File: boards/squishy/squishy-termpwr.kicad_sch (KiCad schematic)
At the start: 23 parts, among them J7 syzygy_standard_x1, Q3 Q_NMOS_PMOS_D1G2S2D2G1S1, U1 LFE5U-45F-8BG256, U11 AD7091R-5, U12 INAx180

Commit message: hardware: cleaned up the schematics a bit and made them more unified
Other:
- company: (none) -> Shrine Maiden Heavy Industries
- title: (none) -> Squishy - Multitool - Termination Power / Expansion
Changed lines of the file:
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@@
 (kicad_sch (version 20211123) (generator eeschema)
-  (paper "A4")
+  (paper "A3")
+  (title_block
+    (title "Squishy - Multitool - Termination Power / Expansion")
+    (date "2021-12-21")
+    (rev "2")
+    (company "Shrine Maiden Heavy Industries")
+    (comment 1 "License:  CERN-OHL-S")
+    (comment 2 "© 2020 Aki 'lethalbit' Van Ness, et. al.")
+    (comment 3 "SCSI PHY Termination power managment and expansion header")
+    (comment 4 "Squishy - SCSI multitool and gateware library")
+  )
   (junction (at 21.59 66.04) (diameter 0) (color 0 0 0 0)
   )

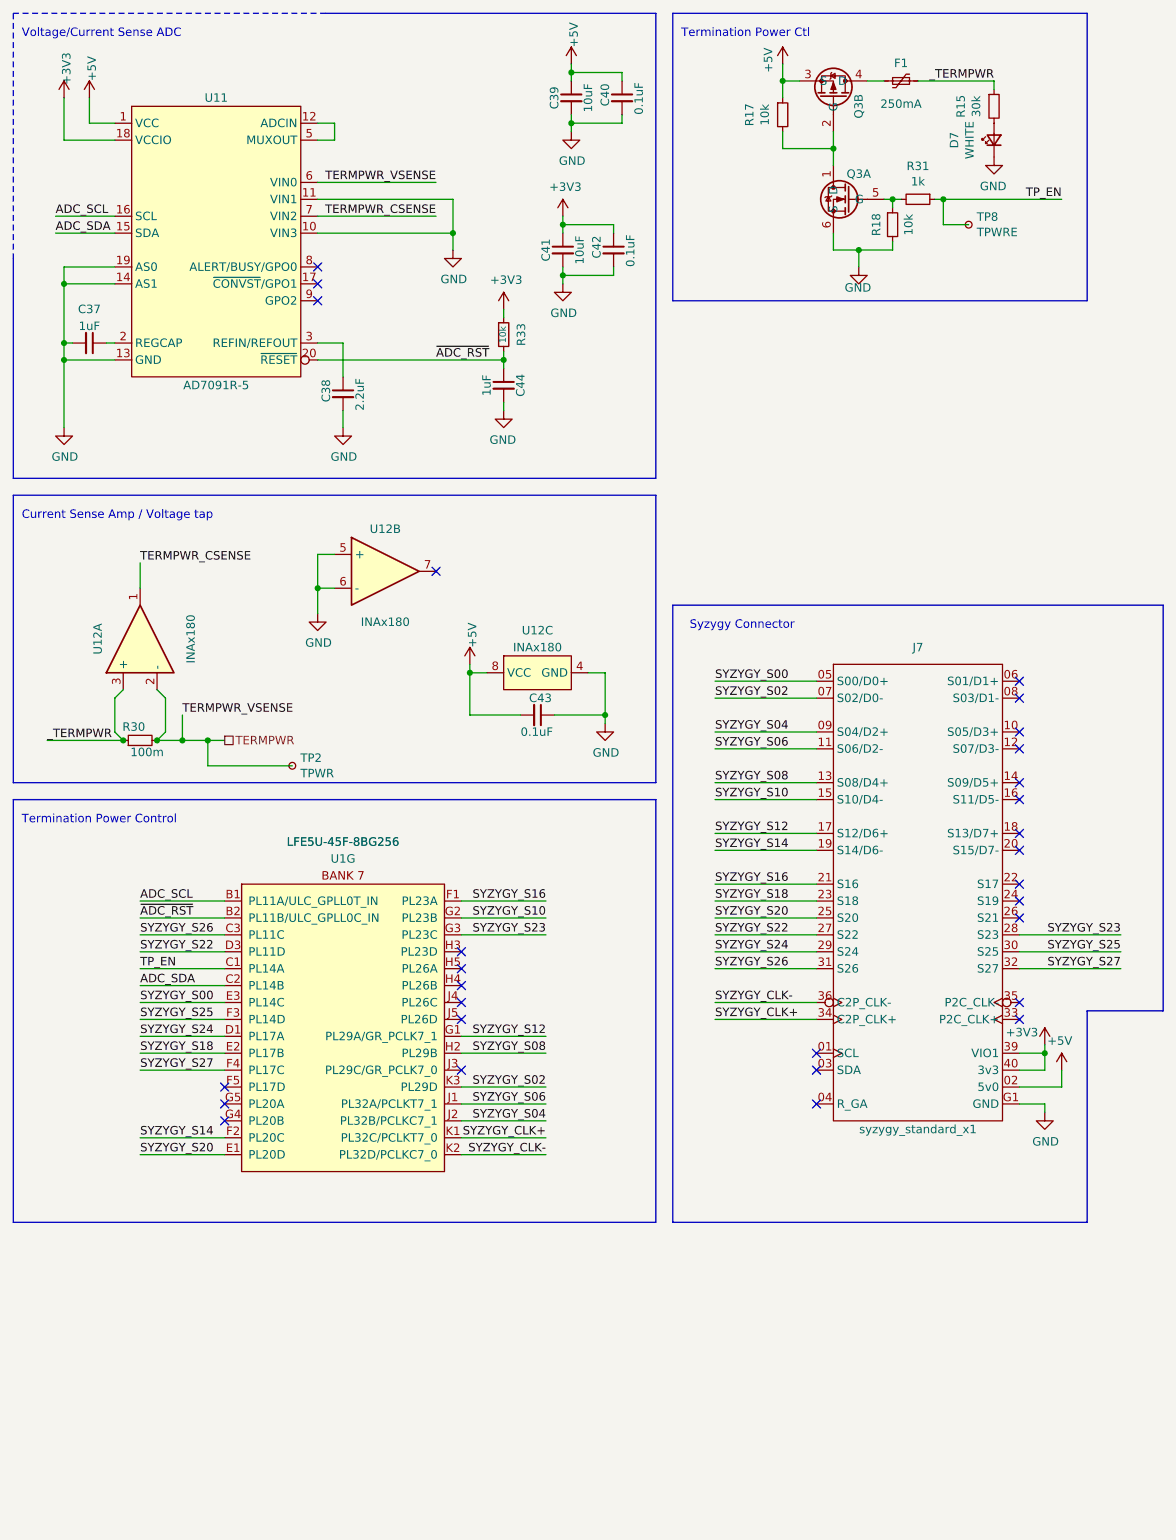
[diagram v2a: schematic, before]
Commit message: hardware: removed the syszygy connector
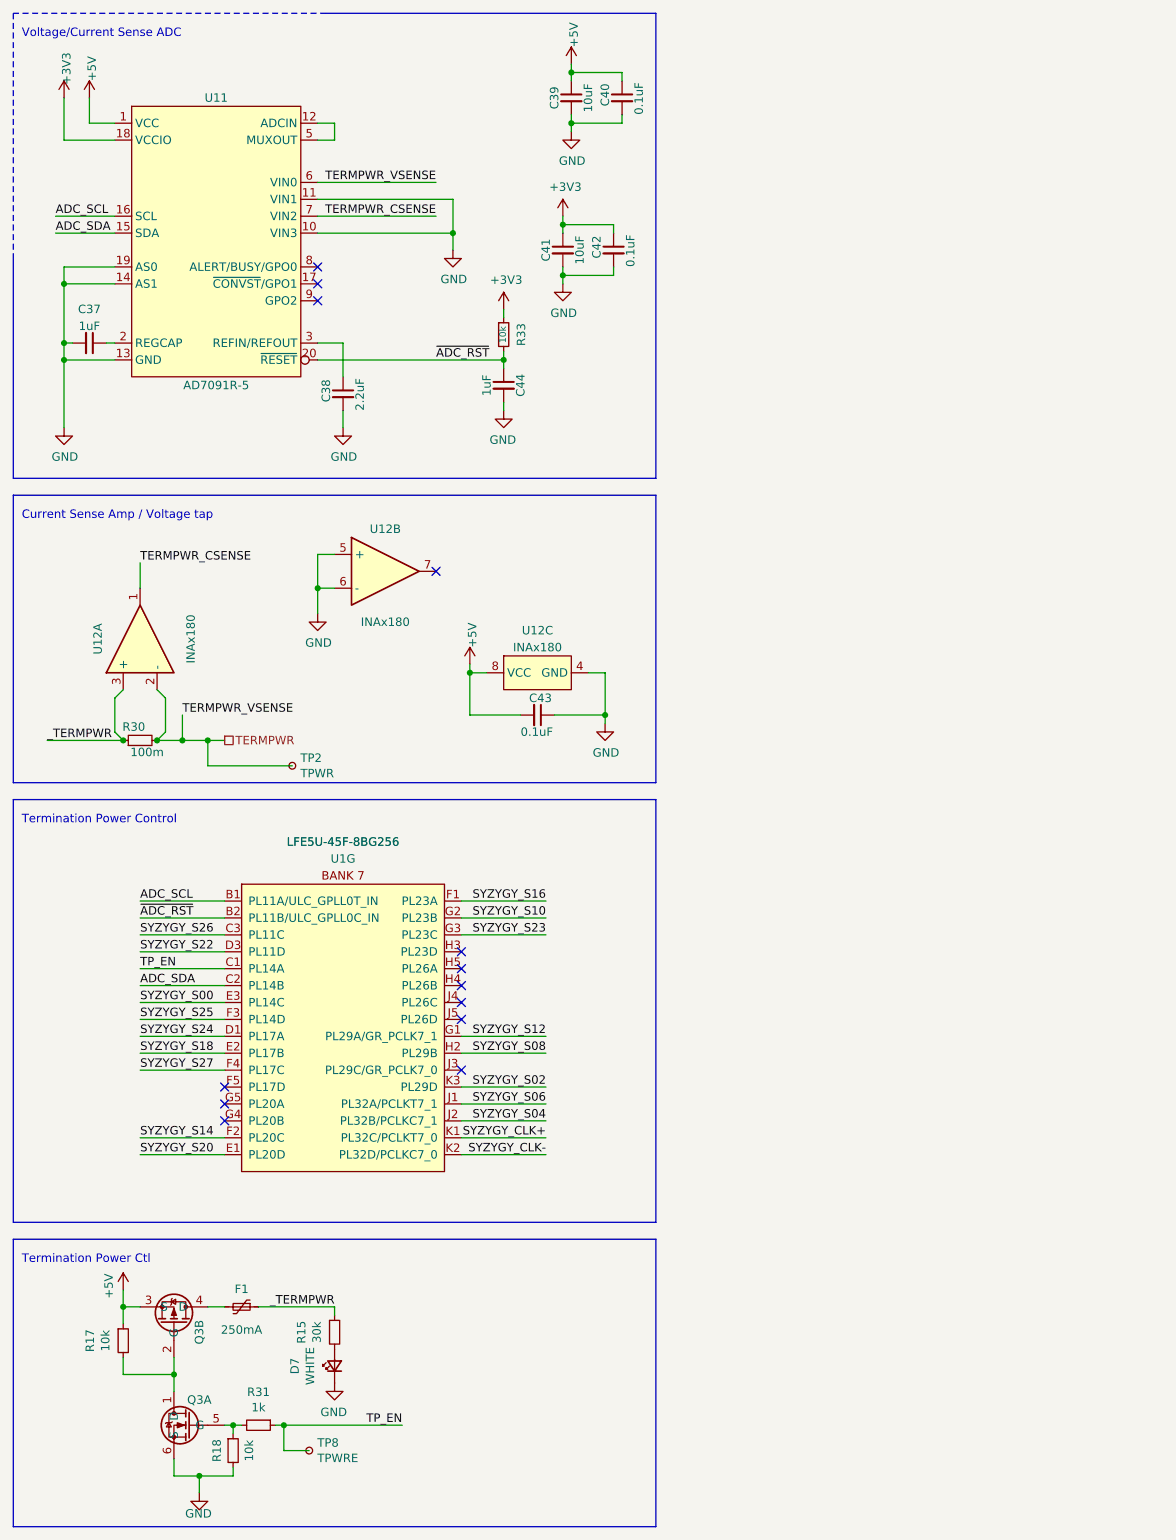
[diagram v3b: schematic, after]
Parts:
- removed J7: syzygy_standard_x1, lethalbit-connectors:syzygy_standard_x1, symbol lethalbit-connectors:syzygy_standard_x1
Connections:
- no-connect marks 29 -> 13
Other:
- note removed: "Syzygy Connector"
- moved on the sheet: D7, F1, Q3A, Q3B, R15, R17, R18, R31, TP8

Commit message: hardware: update fuse symbol footprint
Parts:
- F1: footprint Fuse:Fuse_1210_3225Metric_Castellated -> Fuse:Fuse_1210_3225Metric
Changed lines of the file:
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@@
     (property "Reference" "F1" (id 0) (at 48.26 205.613 90))
     (property "Value" "250mA" (id 1) (at 48.26 211.7344 90))
-    (property "Footprint" "Fuse:Fuse_1210_3225Metric_Castellated" (id 2) (at 43.18 209.55 0)
+    (property "Footprint" "Fuse:Fuse_1210_3225Metric" (id 2) (at 43.18 209.55 0)
       (effects (font (size 1.27 1.27)) (justify left) hide)
     )

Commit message: hardware: some ERC cleanup
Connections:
- net SYZYGY_CLK+: no longer names the net of U1.K1 (PL32C/PCLKT7_0)
- net SYZYGY_CLK-: no longer names the net of U1.K2 (PL32D/PCLKC7_0)
- net SYZYGY_S00: no longer names the net of U1.E3 (PL14C)
- net SYZYGY_S02: no longer names the net of U1.K3 (PL29D)
- net SYZYGY_S04: no longer names the net of U1.J2 (PL32B/PCLKC7_1)
- net SYZYGY_S06: no longer names the net of U1.J1 (PL32A/PCLKT7_1)
- net SYZYGY_S08: no longer names the net of U1.H2 (PL29B)
- net SYZYGY_S10: no longer names the net of U1.G2 (PL23B)
- net SYZYGY_S12: no longer names the net of U1.G1 (PL29A/GR_PCLK7_1)
- net SYZYGY_S14: no longer names the net of U1.F2 (PL20C)
- net SYZYGY_S16: no longer names the net of U1.F1 (PL23A)
- net SYZYGY_S18: no longer names the net of U1.E2 (PL17B)
- net SYZYGY_S20: no longer names the net of U1.E1 (PL20D)
- net SYZYGY_S22: no longer names the net of U1.D3 (PL11D)
- net SYZYGY_S23: no longer names the net of U1.G3 (PL23C)
- net SYZYGY_S24: no longer names the net of U1.D1 (PL17A)
- net SYZYGY_S25: no longer names the net of U1.F3 (PL14D)
- net SYZYGY_S26: no longer names the net of U1.C3 (PL11C)
- net SYZYGY_S27: no longer names the net of U1.F4 (PL17C)
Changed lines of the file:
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@@
-    (stroke (width 0) (type default) (color 0 0 0 0))
-  )
-  (wire (pts (xy 93.98 147.32) (xy 81.28 147.32))
     (stroke (width 0) (type default) (color 0 0 0 0))
   )
@@
     (stroke (width 0) (type default) (color 0 0 0 0))
   )
-  (wire (pts (xy 93.98 167.64) (xy 81.28 167.64))
-    (stroke (width 0) (type default) (color 0 0 0 0))
-  )
   (wire (pts (xy 63.5 63.5) (xy 63.5 68.58))
     (stroke (width 0) (type default) (color 0 0 0 0))
@@
     (stroke (width 0) (type solid) (color 0 0 0 0))
   )
-  (wire (pts (xy 33.02 167.64) (xy 45.72 167.64))
-    (stroke (width 0) (type default) (color 0 0 0 0))
-  )
-  (wire (pts (xy 33.02 170.18) (xy 45.72 170.18))
-    (stroke (width 0) (type default) (color 0 0 0 0))
-  )
   (wire (pts (xy 35.56 123.19) (xy 36.83 121.92))
     (stroke (width 0) (type default) (color 0 0 0 0))
@@
     (stroke (width 0) (type default) (color 0 0 0 0))
   )
-  (wire (pts (xy 93.98 152.4) (xy 81.28 152.4))
-    (stroke (width 0) (type default) (color 0 0 0 0))
-  )
-  (wire (pts (xy 33.02 152.4) (xy 45.72 152.4))
-    (stroke (width 0) (type default) (color 0 0 0 0))
-  )
   (wire (pts (xy 21.59 54.61) (xy 21.59 63.5))
     (stroke (width 0) (type default) (color 0 0 0 0))
   )
-  (wire (pts (xy 81.28 185.42) (xy 93.98 185.42))
-    (stroke (width 0) (type default) (color 0 0 0 0))
-  )
   (wire (pts (xy 97.79 22.86) (xy 97.79 24.13))
     (stroke (width 0) (type default) (color 0 0 0 0))
@@
     (stroke (width 0) (type default) (color 0 0 0 0))
   )
-  (wire (pts (xy 93.98 180.34) (xy 81.28 180.34))
-    (stroke (width 0) (type default) (color 0 0 0 0))
-  )
   (wire (pts (xy 21.59 63.5) (xy 22.86 63.5))
     (stroke (width 0) (type default) (color 0 0 0 0))
@@
     (stroke (width 0) (type default) (color 0 0 0 0))
   )
-  (wire (pts (xy 33.02 182.88) (xy 45.72 182.88))
-    (stroke (width 0) (type default) (color 0 0 0 0))
-  )
   (wire (pts (xy 30.48 208.28) (xy 30.48 205.74))
     (stroke (width 0) (type solid) (color 0 0 0 0))
@@
     (stroke (width 0) (type default) (color 0 0 0 0))
   )
-  (wire (pts (xy 33.02 165.1) (xy 45.72 165.1))
-    (stroke (width 0) (type default) (color 0 0 0 0))
-  )
   (wire (pts (xy 20.32 44.45) (xy 29.21 44.45))
     (stroke (width 0) (type default) (color 0 0 0 0))
@@
     (stroke (width 0) (type default) (color 0 0 0 0))
   )
-  (wire (pts (xy 33.02 154.94) (xy 45.72 154.94))
-    (stroke (width 0) (type default) (color 0 0 0 0))
-  )
-  (wire (pts (xy 33.02 185.42) (xy 45.72 185.42))
-    (stroke (width 0) (type default) (color 0 0 0 0))
-  )
   (wire (pts (xy 46.99 226.06) (xy 46.99 227.33))
     (stroke (width 0) (type default) (color 0 0 0 0))
@@
     (stroke (width 0) (type default) (color 0 0 0 0))
   )
-  (wire (pts (xy 93.98 175.26) (xy 81.28 175.26))
-    (stroke (width 0) (type default) (color 0 0 0 0))
-  )
   (wire (pts (xy 97.79 30.48) (xy 97.79 31.75))
     (stroke (width 0) (type default) (color 0 0 0 0))
@@
     (stroke (width 0) (type default) (color 0 0 0 0))
   )
-  (wire (pts (xy 93.98 149.86) (xy 81.28 149.86))
-    (stroke (width 0) (type default) (color 0 0 0 0))
-  )
   (wire (pts (xy 45.72 208.28) (xy 43.18 208.28))
     (stroke (width 0) (type solid) (color 0 0 0 0))
@@
     (stroke (width 0) (type default) (color 0 0 0 0))
   )
-  (wire (pts (xy 93.98 170.18) (xy 81.28 170.18))
-    (stroke (width 0) (type default) (color 0 0 0 0))
-  )
   (polyline (pts (xy 110.49 83.82) (xy 13.97 83.82))
     (stroke (width 0) (type default) (color 0 0 0 0))
@@
     (stroke (width 0) (type default) (color 0 0 0 0))
   )
-  (wire (pts (xy 33.02 162.56) (xy 45.72 162.56))
-    (stroke (width 0) (type default) (color 0 0 0 0))
-  )
   (wire (pts (xy 96.52 53.34) (xy 96.52 54.61))
     (stroke (width 0) (type default) (color 0 0 0 0))
@@
   )
   (wire (pts (xy 38.1 233.68) (xy 41.91 233.68))
-    (stroke (width 0) (type default) (color 0 0 0 0))
-  )
-  (wire (pts (xy 33.02 172.72) (xy 45.72 172.72))
     (stroke (width 0) (type default) (color 0 0 0 0))
   )
@@
     (stroke (width 0) (type solid) (color 0 0 0 0))
   )
-  (wire (pts (xy 81.28 182.88) (xy 93.98 182.88))
-    (stroke (width 0) (type default) (color 0 0 0 0))
-  )
   (wire (pts (xy 39.37 123.19) (xy 35.56 123.19))
     (stroke (width 0) (type default) (color 0 0 0 0))
@@
   )
   (wire (pts (xy 29.21 30.48) (xy 25.4 30.48))
-    (stroke (width 0) (type default) (color 0 0 0 0))
-  )
-  (wire (pts (xy 93.98 177.8) (xy 81.28 177.8))
     (stroke (width 0) (type default) (color 0 0 0 0))
   )
@@
     (effects (font (size 1.27 1.27)) (justify left bottom))
   )
-  (label "SYZYGY_S20" (at 33.02 185.42 0)
-    (effects (font (size 1.27 1.27)) (justify left bottom))
-  )
-  (label "SYZYGY_S14" (at 33.02 182.88 0)
-    (effects (font (size 1.27 1.27)) (justify left bottom))
-  )
-  (label "SYZYGY_CLK+" (at 93.98 182.88 180)
-    (effects (font (size 1.27 1.27)) (justify right bottom))
-  )
   (label "ADC_SCL" (at 33.02 147.32 0)
     (effects (font (size 1.27 1.27)) (justify left bottom))
@@
     (effects (font (size 1.27 1.27)) (justify right bottom))
   )
-  (label "SYZYGY_S25" (at 33.02 165.1 0)
-    (effects (font (size 1.27 1.27)) (justify left bottom))
-  )
   (label "TP_EN" (at 72.39 226.06 180)
     (effects (font (size 1.27 1.27)) (justify right bottom))
@@
     (effects (font (size 1.27 1.27)) (justify left bottom))
   )
-  (label "SYZYGY_S06" (at 93.98 177.8 180)
-    (effects (font (size 1.27 1.27)) (justify right bottom))
-  )
   (label "ADC_SCL" (at 20.32 44.45 0)
     (effects (font (size 1.27 1.27)) (justify left bottom))
   )
-  (label "SYZYGY_S26" (at 33.02 152.4 0)
-    (effects (font (size 1.27 1.27)) (justify left bottom))
-  )
-  (label "SYZYGY_S10" (at 93.98 149.86 180)
-    (effects (font (size 1.27 1.27)) (justify right bottom))
-  )
   (label "~{ADC_RST}" (at 33.02 149.86 0)
     (effects (font (size 1.27 1.27)) (justify left bottom))
@@
   (label "_TERMPWR" (at 19.05 123.19 0)
     (effects (font (size 1.27 1.27)) (justify left bottom))
-  )
-  (label "SYZYGY_S02" (at 93.98 175.26 180)
-    (effects (font (size 1.27 1.27)) (justify right bottom))
-  )
-  (label "SYZYGY_S08" (at 93.98 170.18 180)
-    (effects (font (size 1.27 1.27)) (justify right bottom))
   )
   (label "TERMPWR_CSENSE" (at 77.47 44.45 180)
     (effects (font (size 1.27 1.27)) (justify right bottom))
   )
-  (label "SYZYGY_S27" (at 33.02 172.72 0)
-    (effects (font (size 1.27 1.27)) (justify left bottom))
-  )
-  (label "SYZYGY_S00" (at 33.02 162.56 0)
-    (effects (font (size 1.27 1.27)) (justify left bottom))
-  )
-  (label "SYZYGY_S12" (at 93.98 167.64 180)
-    (effects (font (size 1.27 1.27)) (justify right bottom))
-  )
-  (label "SYZYGY_S04" (at 93.98 180.34 180)
-    (effects (font (size 1.27 1.27)) (justify right bottom))
-  )
-  (label "SYZYGY_S18" (at 33.02 170.18 0)
-    (effects (font (size 1.27 1.27)) (justify left bottom))
-  )
-  (label "SYZYGY_S22" (at 33.02 154.94 0)
-    (effects (font (size 1.27 1.27)) (justify left bottom))
-  )
-  (label "SYZYGY_S16" (at 93.98 147.32 180)
-    (effects (font (size 1.27 1.27)) (justify right bottom))
-  )
   (label "_TERMPWR" (at 62.23 208.28 180)
     (effects (font (size 1.27 1.27)) (justify right bottom))
@@
     (effects (font (size 1.27 1.27)) (justify left bottom))
   )
-  (label "SYZYGY_S24" (at 33.02 167.64 0)
-    (effects (font (size 1.27 1.27)) (justify left bottom))
-  )
   (label "ADC_SDA" (at 33.02 160.02 0)
     (effects (font (size 1.27 1.27)) (justify left bottom))
   )
-  (label "SYZYGY_S23" (at 93.98 152.4 180)
-    (effects (font (size 1.27 1.27)) (justify right bottom))
-  )
-  (label "SYZYGY_CLK-" (at 93.98 185.42 180)
-    (effects (font (size 1.27 1.27)) (justify right bottom))
-  )
   (label "TERMPWR_CSENSE" (at 33.02 96.52 0)

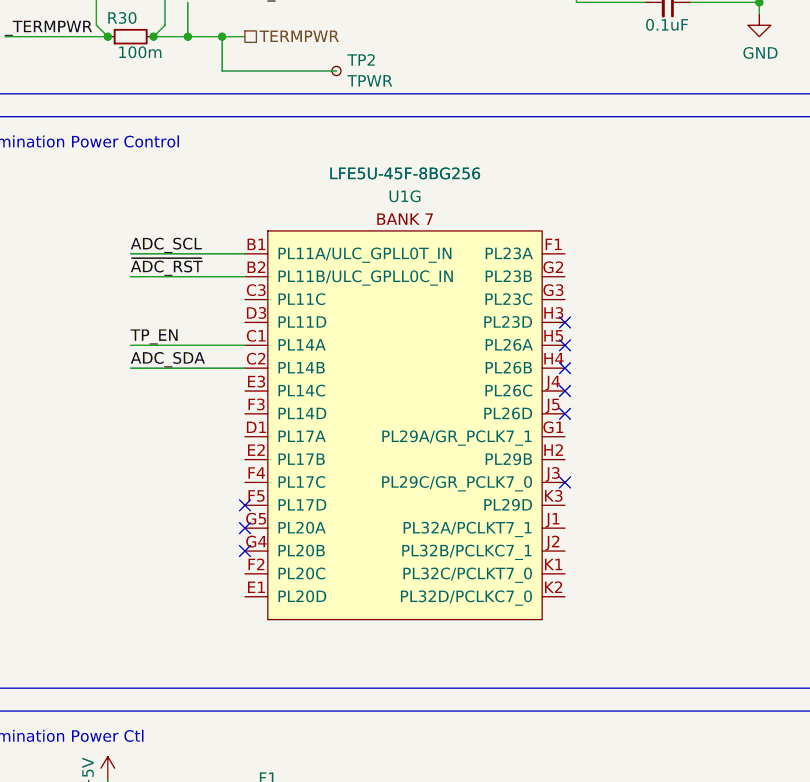
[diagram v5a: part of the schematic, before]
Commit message: hardware: started gutting the old FPGA in preparation to migrate to the new FPGA
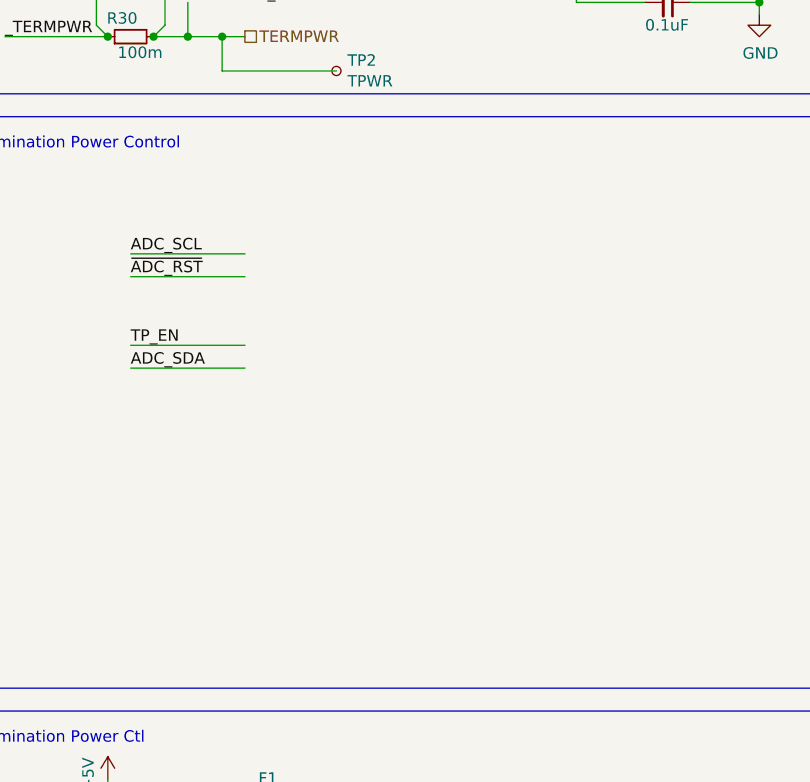
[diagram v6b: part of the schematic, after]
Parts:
- removed U1: LFE5U-45F-8BG256, lethalbit:BGA-256_16x16_14.0x14.0mm, symbol lethalbit:LFE5U-45F-8BG381
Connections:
- no-connect marks 13 -> 4
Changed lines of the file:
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@@
   )
   (no_connect (at 77.47 97.79))
-  (no_connect (at 45.72 175.26))
-  (no_connect (at 81.28 160.02))
-  (no_connect (at 45.72 177.8))
-  (no_connect (at 81.28 154.94))
   (no_connect (at 59.69 54.61))
-  (no_connect (at 81.28 157.48))
-  (no_connect (at 45.72 180.34))
   (no_connect (at 59.69 57.15))
-  (no_connect (at 81.28 162.56))
   (no_connect (at 59.69 52.07))
-  (no_connect (at 81.28 165.1))
-  (no_connect (at 81.28 172.72))
   (wire (pts (xy 21.59 52.07) (xy 21.59 54.61))
     (stroke (width 0) (type default) (color 0 0 0 0))
@@
     (pin "1")
   )
-  (symbol (lib_id "lethalbit:LFE5U-45F-8BG381") (at 63.5 147.32 0) (unit 7)
-    (in_bom yes) (on_board yes)
-    (property "Reference" "U1" (id 0) (at 63.5 140.97 0))
-    (property "Value" "LFE5U-45F-8BG256" (id 1) (at 63.5 138.43 0))
-    (property "Footprint" "lethalbit:BGA-256_16x16_14.0x14.0mm" (id 2) (at 63.5 132.08 0)
-      (effects (font (size 1.27 1.27)) hide)
-    )
-    (property "Datasheet" "https://4donline.ihs.com/images/VipMasterIC/IC/LATT/LATT-S-A0011156806/LATT-S-A0011461202-1.pdf?hkey=CECEF36DEECDED6468708AAF2E19C0C6" (id 3) (at 63.5 129.54 0)
-      (effects (font (size 1.27 1.27)) hide)
-    )
-    (property "MFR" "Lattice" (id 4) (at 63.5 134.62 0)
-      (effects (font (size 1.27 1.27)) hide)
-    )
-    (property "MPN" "LFE5U-45F-8BG256" (id 5) (at 63.5 138.43 0))
-    (pin "B1")
-    (pin "B2")
-    (pin "C1")
-    (pin "C2")
-    (pin "C3")
-    (pin "D1")
-    (pin "D3")
-    (pin "E1")
-    (pin "E2")
-    (pin "E3")
-    (pin "F1")
-    (pin "F2")
-    (pin "F3")
-    (pin "F4")
-    (pin "F5")
-    (pin "G1")
-    (pin "G2")
-    (pin "G3")
-    (pin "G4")
-    (pin "G5")
-    (pin "H2")
-    (pin "H3")
-    (pin "H4")
-    (pin "H5")
-    (pin "J1")
-    (pin "J2")
-    (pin "J3")
-    (pin "J4")
-    (pin "J5")
-    (pin "K1")
-    (pin "K2")
-    (pin "K3")
-  )
   (symbol (lib_id "Device:R_Small") (at 46.99 229.87 0) (unit 1)
